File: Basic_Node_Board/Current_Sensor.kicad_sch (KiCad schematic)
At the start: 0 parts

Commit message: Add INA220 current sensor to schematic
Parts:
- added U1: INA220AIDGSR, PROVE:DGS10, symbol INA220:INA220AIDGSR
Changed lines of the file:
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@@
 	(generator_version "8.0")
 	(paper "A4")
+	(symbol
+		(lib_id "INA220:INA220AIDGSR")
+		(at 60.96 44.45 0)
+		(unit 1)
+		(exclude_from_sim no)
+		(in_bom yes)
+		(on_board yes)
+		(dnp no)
+		(fields_autoplaced yes)
+		(property "Reference" "U1"
+			(at 88.9 34.29 0)
+			(effects
+				(font
+					(size 1.524 1.524)
+				)
+			)
+		)
+		(property "Value" "INA220AIDGSR"
+			(at 88.9 36.83 0)
+			(effects
+				(font
+					(size 1.524 1.524)
+				)
+			)
+		)
+		(property "Footprint" "PROVE:DGS10"
+			(at 60.96 44.45 0)
+			(effects
+				(font
+					(size 1.27 1.27)
+					(italic yes)
+				)
+				(hide yes)
+			)
+		)
+		(property "Datasheet" "INA220AIDGSR"
+			(at 60.96 44.45 0)
+			(effects
+				(font
+					(size 1.27 1.27)
+					(italic yes)
+				)
+				(hide yes)
+			)
+		)
+		(property "Description" ""
+			(at 60.96 44.45 0)
+			(effects
+				(font
+					(size 1.27 1.27)
+				)
+				(hide yes)
+			)
+		)
+		(pin "4"
+		)
+		(pin "9"
+		)
+		(pin "6"
+		)
+		(pin "2"
+		)
+		(pin "1"
+		)
+		(pin "8"
+		)
+		(pin "10"
+		)
+		(pin "5"
+		)
+		(pin "3"
+		)
+		(pin "7"
+		)
+		(instances
+			(project "Basic_Node_Board"
+				(path "/9602f2a9-59de-4c89-af09-0033871e87a5/171b48c4-31ba-4ad4-b68c-0c27aedd5528"
+					(reference "U1")
+					(unit 1)
+				)
+			)
+		)
+	)
 )

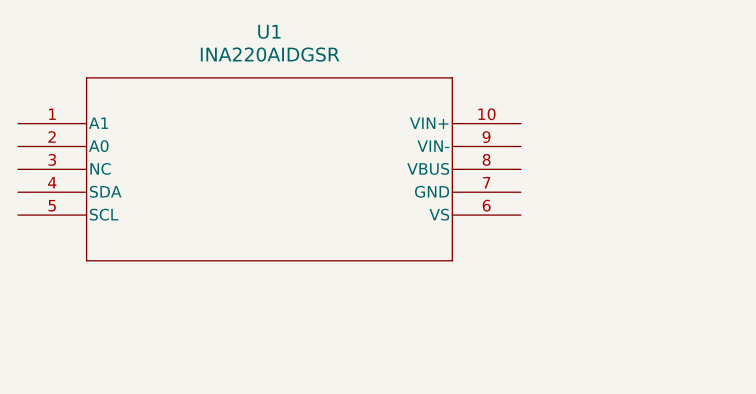
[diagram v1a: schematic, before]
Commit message: Update schematics to use PROVE HTTP lib
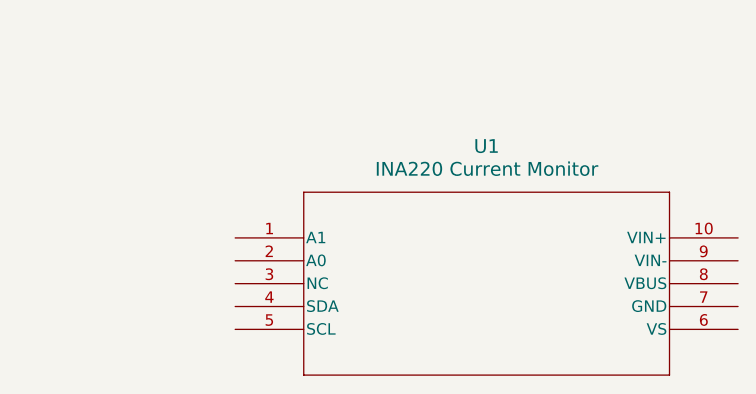
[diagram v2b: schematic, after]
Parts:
- removed U1: INA220AIDGSR, PROVE:DGS10, symbol INA220:INA220AIDGSR
- added U1: INA220 Current Monitor, PROVE:DGS10, symbol PROVE:INA220 Current Monitor
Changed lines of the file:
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@@
 	(paper "A4")
 	(symbol
-		(lib_id "INA220:INA220AIDGSR")
-		(at 60.96 44.45 0)
+		(lib_id "PROVE:INA220 Current Monitor")
+		(at 85.09 57.15 0)
 		(unit 1)
-		(exclude_from_sim no)
+		(exclude_from_sim yes)
 		(in_bom yes)
 		(on_board yes)
@@
 		(fields_autoplaced yes)
 		(property "Reference" "U1"
-			(at 88.9 34.29 0)
+			(at 113.03 46.99 0)
 			(effects
 				(font
@@
 			)
 		)
-		(property "Value" "INA220AIDGSR"
-			(at 88.9 36.83 0)
+		(property "Value" "INA220 Current Monitor"
+			(at 113.03 49.53 0)
 			(effects
 				(font
@@
 		)
 		(property "Footprint" "PROVE:DGS10"
-			(at 60.96 44.45 0)
+			(at 85.09 57.15 0)
 			(effects
 				(font
@@
 			)
 		)
-		(property "Datasheet" "INA220AIDGSR"
-			(at 60.96 44.45 0)
+		(property "Datasheet" "http://138.2.231.237:8080/en/part/1/info"
+			(at 85.09 57.15 0)
 			(effects
 				(font
@@
 			)
 		)
-		(property "Description" ""
-			(at 60.96 44.45 0)
+		(property "Description" "IC CURRENT MONITOR 1% 10VSSOP"
+			(at 85.09 57.15 0)
+			(effects
+				(font
+					(size 1.27 1.27)
+				)
+				(hide yes)
+			)
+		)
+		(property "Category" "IC/Sensor"
+			(at 85.09 57.15 0)
+			(effects
+				(font
+					(size 1.27 1.27)
+				)
+				(hide yes)
+			)
+		)
+		(property "MPN" "INA220AIDGSR"
+			(at 85.09 57.15 0)
+			(effects
+				(font
+					(size 1.27 1.27)
+				)
+				(hide yes)
+			)
+		)
+		(property "Manufacturer" "Texas Instruments"
+			(at 85.09 57.15 0)
+			(effects
+				(font
+					(size 1.27 1.27)
+				)
+				(hide yes)
+			)
+		)
+		(property "Manufacturing Status" "Active"
+			(at 85.09 57.15 0)
+			(effects
+				(font
+					(size 1.27 1.27)
+				)
+				(hide yes)
+			)
+		)
+		(property "Part-DB Footprint" "10VSSOP"
+			(at 85.09 57.15 0)
+			(effects
+				(font
+					(size 1.27 1.27)
+				)
+				(hide yes)
+			)
+		)
+		(property "Part-DB ID" "1"
+			(at 85.09 57.15 0)
 			(effects
 				(font
@@
 		(pin "4"
 		)
+		(pin "2"
+		)
+		(pin "10"
+		)
+		(pin "3"
+		)
+		(pin "1"
+		)
+		(pin "5"
+		)
 		(pin "9"
+		)
+		(pin "8"
+		)
+		(pin "7"
 		)
 		(pin "6"
 		)
-		(pin "2"
-		)
-		(pin "1"
-		)
-		(pin "8"
-		)
-		(pin "10"
-		)
-		(pin "5"
-		)
-		(pin "3"
-		)
-		(pin "7"
-		)
 		(instances

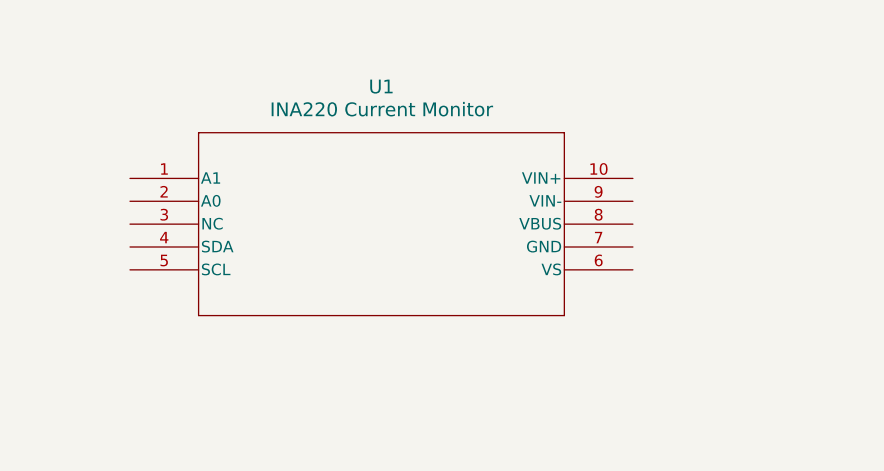
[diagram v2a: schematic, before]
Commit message: current sensor schematic added
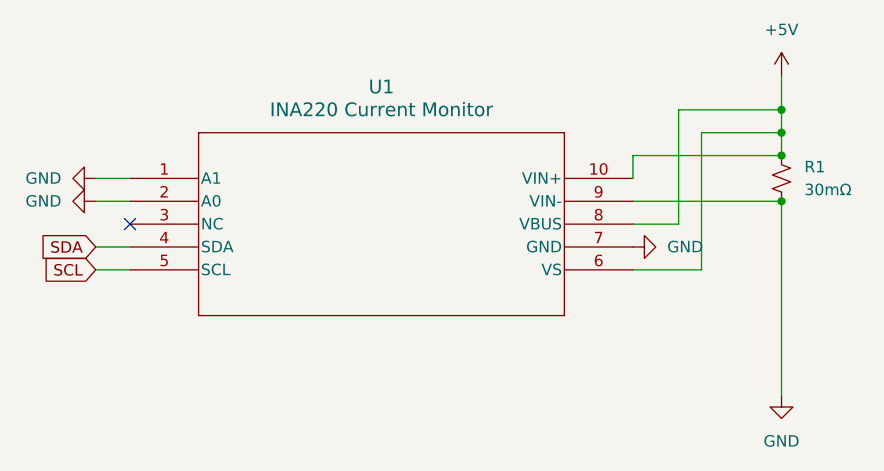
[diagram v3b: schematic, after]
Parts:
- added R1: 30mΩ, symbol Device:R_Small_US
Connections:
- net GND: now reaches U1.1 (A1)
- net GND: now also U1.2 (A0), U1.7 (GND), U1.9 (VIN-), R1.2
- net +5V: now reaches U1.10 (VIN+)
- net +5V: now also U1.6 (VS), U1.8 (VBUS), R1.1
- net SDA: now reaches U1.4 (SDA)
- net SCL: now reaches U1.5 (SCL)
- no-connect marks 0 -> 1

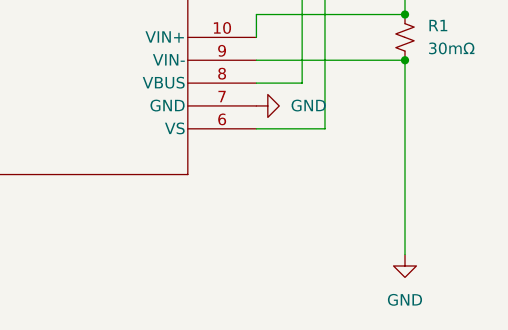
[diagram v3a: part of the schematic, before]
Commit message: updated load symbol
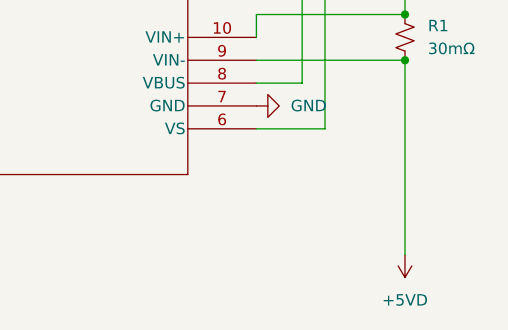
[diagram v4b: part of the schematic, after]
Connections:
- net GND: no longer R1.2, U1.9 (VIN-)
- new net +5VD: R1.2, U1.9 (VIN-)

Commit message: Adding Buck Converter Schematic/Footprints
Added footprints to main pcb. Removing duplicate footprints (might cause problems, we will find out).
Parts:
- U1: footprint PROVE:DGS10 -> (none)
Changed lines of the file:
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@@
 (kicad_sch
-	(version 20231120)
+	(version 20250114)
 	(generator "eeschema")
-	(generator_version "8.0")
+	(generator_version "9.0")
 	(paper "A4")
 	(junction
@@
 			)
 		)
-		(property "Footprint" "PROVE:DGS10"
+		(property "Footprint" ""
 			(at 85.09 57.15 0)
 			(effects

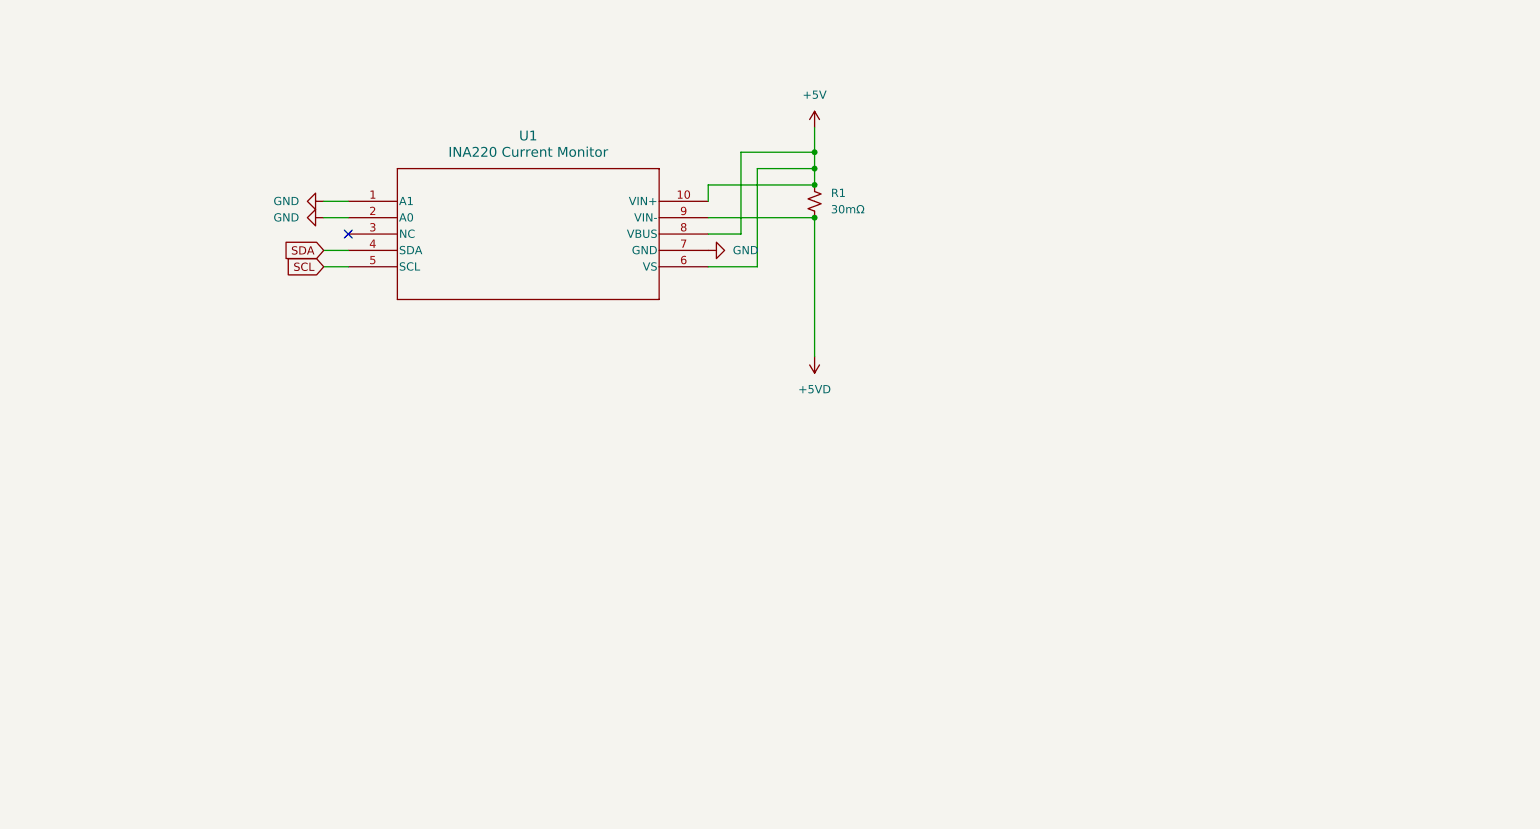
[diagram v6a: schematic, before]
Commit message: Power Distribution PCB KiCAD Schematic
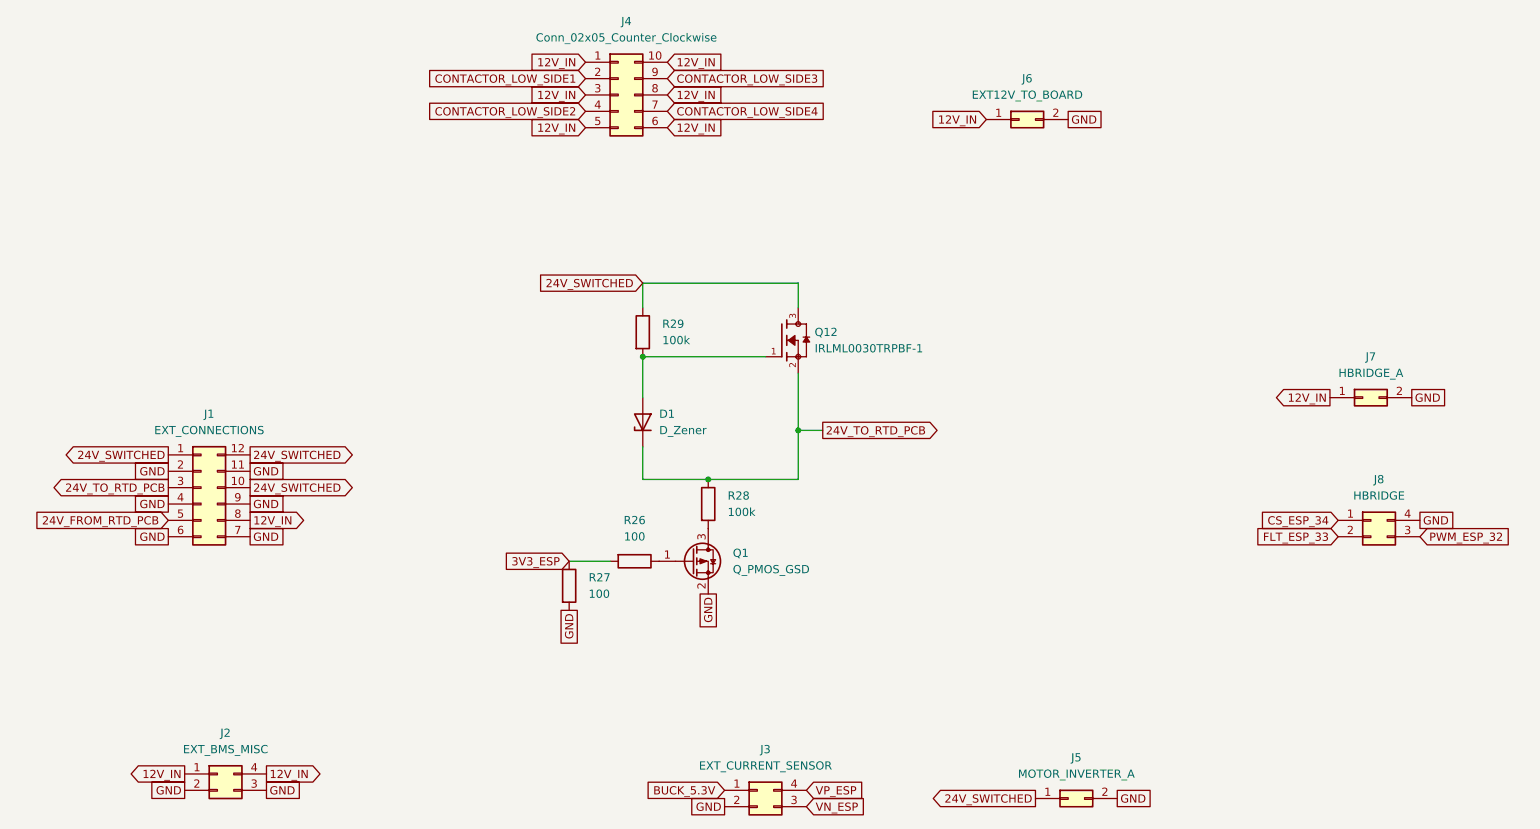
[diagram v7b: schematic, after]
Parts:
- removed R1: 30mΩ, symbol Device:R_Small_US
- removed U1: INA220 Current Monitor, symbol PROVE:INA220 Current Monitor
- added D1: D_Zener, Diode_THT:D_DO-35_SOD27_P7.62mm_Horizontal, symbol Device:D_Zener
- added J1: EXT_CONNECTIONS, Connector_Molex:Molex_Mini-Fit_Jr_5569-12A2_2x06_P4.20mm_Horizontal, symbol Connector_Generic:Conn_02x06_Counter_Clockwise
- added J2: EXT_BMS_MISC, Connector_Molex:Molex_Mini-Fit_Jr_5569-04A2_2x02_P4.20mm_Horizontal, symbol Connector_Generic:Conn_02x02_Counter_Clockwise
- added J3: EXT_CURRENT_SENSOR, Connector_Molex:Molex_Mini-Fit_Jr_5569-04A2_2x02_P4.20mm_Horizontal, symbol Connector_Generic:Conn_02x02_Counter_Clockwise
- added J4: Conn_02x05_Counter_Clockwise, Connector_Molex:Molex_Mini-Fit_Jr_5569-10A2_2x05_P4.20mm_Horizontal, symbol Connector_Generic:Conn_02x05_Counter_Clockwise
- added J5: MOTOR_INVERTER_A, Custom_Connectors:Anderson_1336G1_RightAngle_2Pin, symbol Connector_Generic:Conn_02x01
- added J6: EXT12V_TO_BOARD, Custom_Connectors:Anderson_1336G1_RightAngle_2Pin, symbol Connector_Generic:Conn_02x01
- added J7: HBRIDGE_A, Custom_Connectors:Anderson_1336G1_RightAngle_2Pin, symbol Connector_Generic:Conn_02x01
- added J8: HBRIDGE, Connector_Molex:Molex_Mini-Fit_Jr_5569-04A2_2x02_P4.20mm_Horizontal, symbol Connector_Generic:Conn_02x02_Counter_Clockwise
- added Q1: Q_PMOS_GSD, Package_SO:SOIC-8_3.9x4.9mm_P1.27mm, symbol Transistor_FET:Q_PMOS_GSD
- added Q12: IRLML0030TRPBF-1, IRLML0030TRPBF-1:SOT95P237X112-3N, symbol IRLML0030TRPBF-1:IRLML0030TRPBF-1
- added R26, R27: 100, Resistor_SMD:R_1206_3216Metric_Pad1.30x1.75mm_HandSolder, symbol Device:R
- added R28, R29: 100k, Resistor_SMD:R_1206_3216Metric_Pad1.30x1.75mm_HandSolder, symbol Device:R
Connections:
- net GND: now also J1.11 (Pin_11), J1.2 (Pin_2), J1.4 (Pin_4), J1.6 (Pin_6), J1.7 (Pin_7), J1.9 (Pin_9), J2.2 (Pin_2), J2.3 (Pin_3), J3.2 (Pin_2), J5.2 (Pin_2), J6.2 (Pin_2), J7.2 (Pin_2), J8.4 (Pin_4), Q1.2 (S), R27.2
- new net: D1.2 (A), Q12.1, R29.2
- new net: Q1.3 (D), R28.2
- new net: Q1.1 (G), R26.1
- new net 12V_IN: J1.8 (Pin_8), J2.1 (Pin_1), J2.4 (Pin_4), J4.1 (Pin_1), J4.10 (Pin_10), J4.3 (Pin_3), J4.5 (Pin_5), J4.6 (Pin_6), J4.8 (Pin_8), J6.1 (Pin_1), J7.1 (Pin_1)
- new net 24V_FROM_RTD_PCB: J1.5 (Pin_5)
- new net 24V_SWITCHED: J1.1 (Pin_1), J1.10 (Pin_10), J1.12 (Pin_12), J5.1 (Pin_1), Q12.3, R29.1
- new net 24V_TO_RTD_PCB: D1.1 (K), J1.3 (Pin_3), Q12.2, R28.1
- new net 3V3_ESP: R26.2, R27.1
- new net BUCK_5.3V: J3.1 (Pin_1)
- new net CONTACTOR_LOW_SIDE1: J4.2 (Pin_2)
- new net CONTACTOR_LOW_SIDE2: J4.4 (Pin_4)
- new net CONTACTOR_LOW_SIDE3: J4.9 (Pin_9)
- new net CONTACTOR_LOW_SIDE4: J4.7 (Pin_7)
- new net CS_ESP_34: J8.1 (Pin_1)
- new net FLT_ESP_33: J8.2 (Pin_2)
- new net PWM_ESP_32: J8.3 (Pin_3)
- new net VN_ESP: J3.3 (Pin_3)
- new net VP_ESP: J3.4 (Pin_4)
- no-connect marks 1 -> 0
